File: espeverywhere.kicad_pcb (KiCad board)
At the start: 2 copper layers, 45 x 51 mm, 39 parts, among them P1 USB_OTG, P3 CONN_01X06, SW2 GPIO0, SW3 RESET, U1 AP2112K-3.3V, U2 ESP-12E, U3 FT230XS

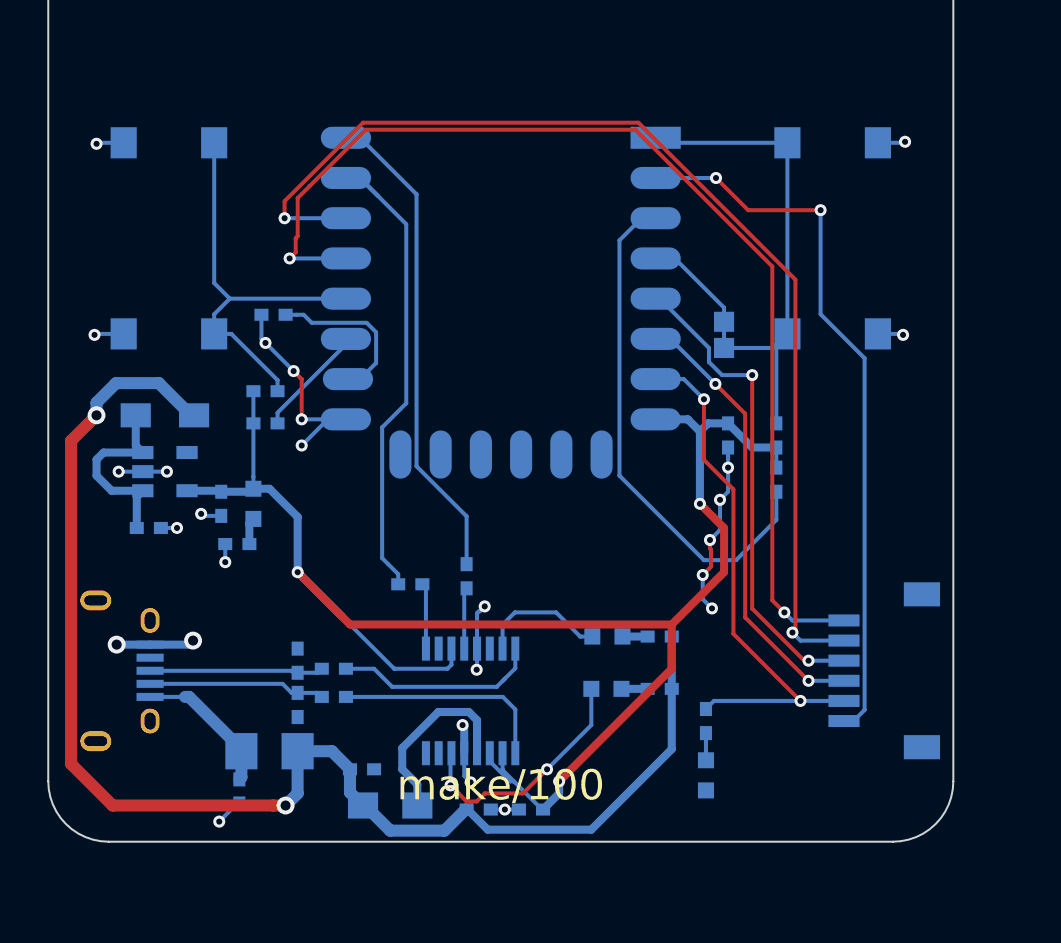
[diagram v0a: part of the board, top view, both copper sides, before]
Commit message: Changed JST-SH-6 to 8 Pin
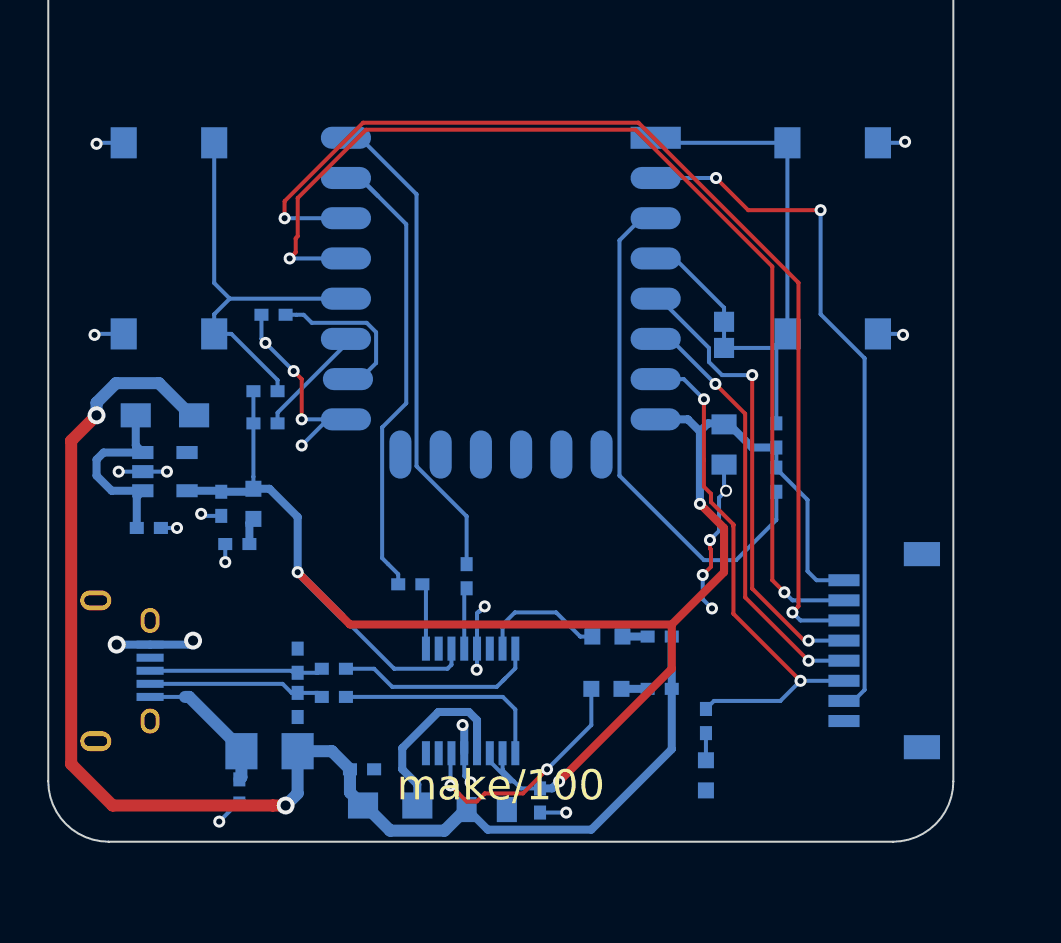
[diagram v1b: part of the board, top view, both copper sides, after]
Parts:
- added G***: LOGO, idlehands_footprints:IdlehandsdevLogo, B.Cu at (138.0, 103.0)
- added G***: LOGO, idlehands_footprints:OSHLogo, B.Cu at (141.2, 124.5)
- C6, C9: footprint project_footprints:C_0402_Hand -> idlehands_footprints:C_0805
- D2: footprint project_footprints:sod323 -> idlehands_footprints:bat20j
- P3: value CONN_01X06 -> CONN_01X08; footprint Connectors_JST_SH:Connectors_JST_SM06B-SRSS-TB -> Connectors_JST_SH:Connectors_JST_SM08B-SRSS-TB
- moved P3 1.00 mm to (141.5, 135.5)
- moved C7 0.64 mm to (124.5, 142.9), turned to 90 degrees
- moved C6 0.49 mm to (133.6, 125.2)
- moved C9 0.40 mm to (121.8, 143.4)
- turned D2 to 180 degrees
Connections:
- P3 pad 1: /GPIO4 -> +3V3
- P3 pad 2: /GPIO5 -> /GPIO4
- P3 pad 3: /GPIO14 -> /GPIO5
- P3 pad 4: /GPIO12 -> /GPIO14
- P3 pad 5: /GPIO13 -> /GPIO12
- P3 pad 6: /ADC -> /GPIO13
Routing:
- net +3V3: track 81.3 -> 87.8 mm
- net /GPIO14: track 25.3 -> 24.3 mm
- net /ADC: track 36.6 -> 35.6 mm
- net /GPIO4: track 55.1 -> 54.1 mm
- net /GPIO12: track 23.0 -> 22.0 mm
- net GND: track 44.8 -> 43.9 mm, vias 26 -> 25
- net /GPIO5: track 55.2 -> 54.5 mm
- net /GPIO13: track 27.5 -> 27.0 mm
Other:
- board text added: "3.3V"
- board text added: "GND"

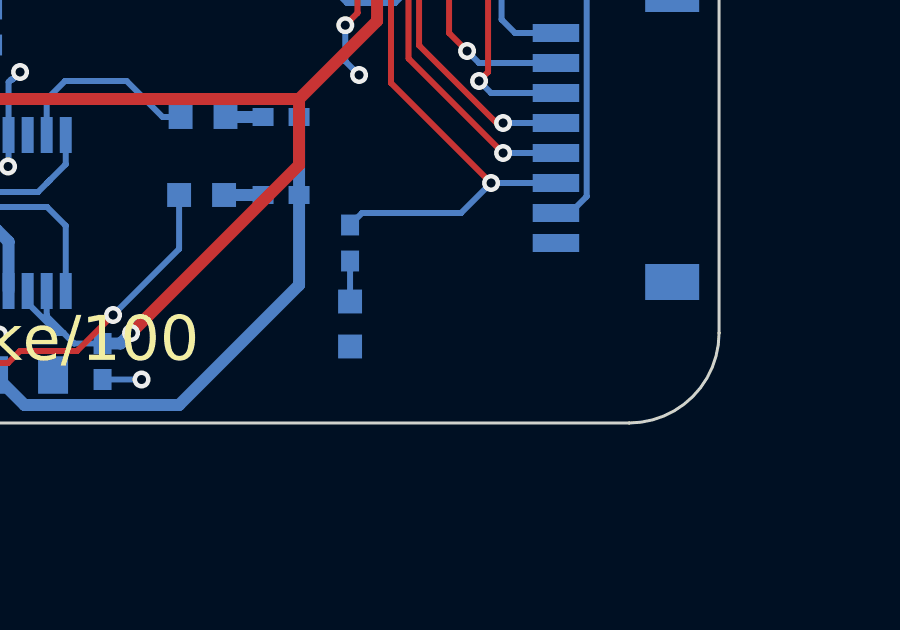
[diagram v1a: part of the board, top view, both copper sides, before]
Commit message: Breakout Board added
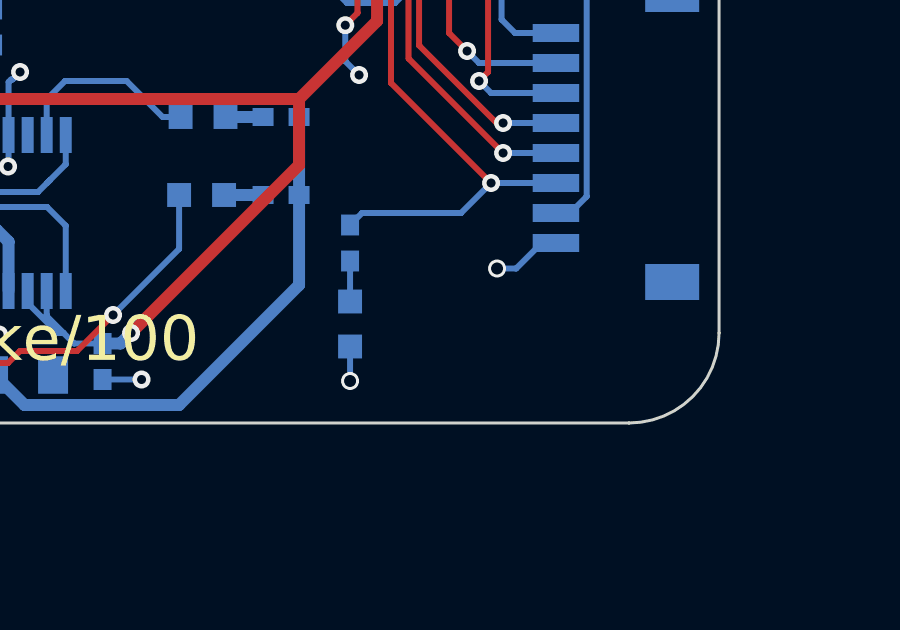
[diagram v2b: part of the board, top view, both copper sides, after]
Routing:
- net GND: track 43.9 -> 47.3 mm, vias 25 -> 27
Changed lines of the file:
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@@
 (kicad_pcb (version 4) (host pcbnew 4.0.4-stable)
   (general
-    (links 0)
-    (no_connects 11)
-    (area 99.949999 93.949999 145.050001 145.050001)
+    (links 84)
+    (no_connects 3)
+    (area 59.425 63.6 186.475001 188.195005)
     (thickness 1.6)
     (drawings 27)
-    (tracks 343)
+    (tracks 349)
     (zones 0)
     (modules 41)
@@
       (drillshape 0)
       (scaleselection 1)
-      (outputdirectory ../espeverywhere/gerbs/))
+      (outputdirectory gerbs/))
   )
   (net 0 "")
@@
   (gr_line (start 103 100) (end 116.5 100) (layer Edge.Cuts) (width 0.1))
   (gr_line (start 100 142) (end 100 103) (layer Edge.Cuts) (width 0.1))
+  (segment (start 132.7 142.4493) (end 132.7 143.6) (width 0.2) (layer B.Cu) (net 1))
+  (via (at 132.7 143.6) (size 0.6) (drill 0.4) (layers F.Cu B.Cu) (net 1))
+  (segment (start 139.5625 139) (end 139.0875 139) (width 0.2) (layer B.Cu) (net 1))
+  (segment (start 139.0875 139) (end 138.2375 139.85) (width 0.2) (layer B.Cu) (net 1))
+  (segment (start 138.2375 139.85) (end 137.6 139.85) (width 0.2) (layer B.Cu) (net 1))
+  (via (at 137.6 139.85) (size 0.6) (drill 0.4) (layers F.Cu B.Cu) (net 1))
   (segment (start 124.45 143.55) (end 125.75 143.55) (width 0.2) (layer B.Cu) (net 1))
   (via (at 125.75 143.55) (size 0.6) (drill 0.3) (layers F.Cu B.Cu) (net 1))
